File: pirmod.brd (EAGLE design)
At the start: 100 x 80 mm, 12 parts, among them IC1 TLC555CD, K1 22V, K2 LSP10, K3 LSP10

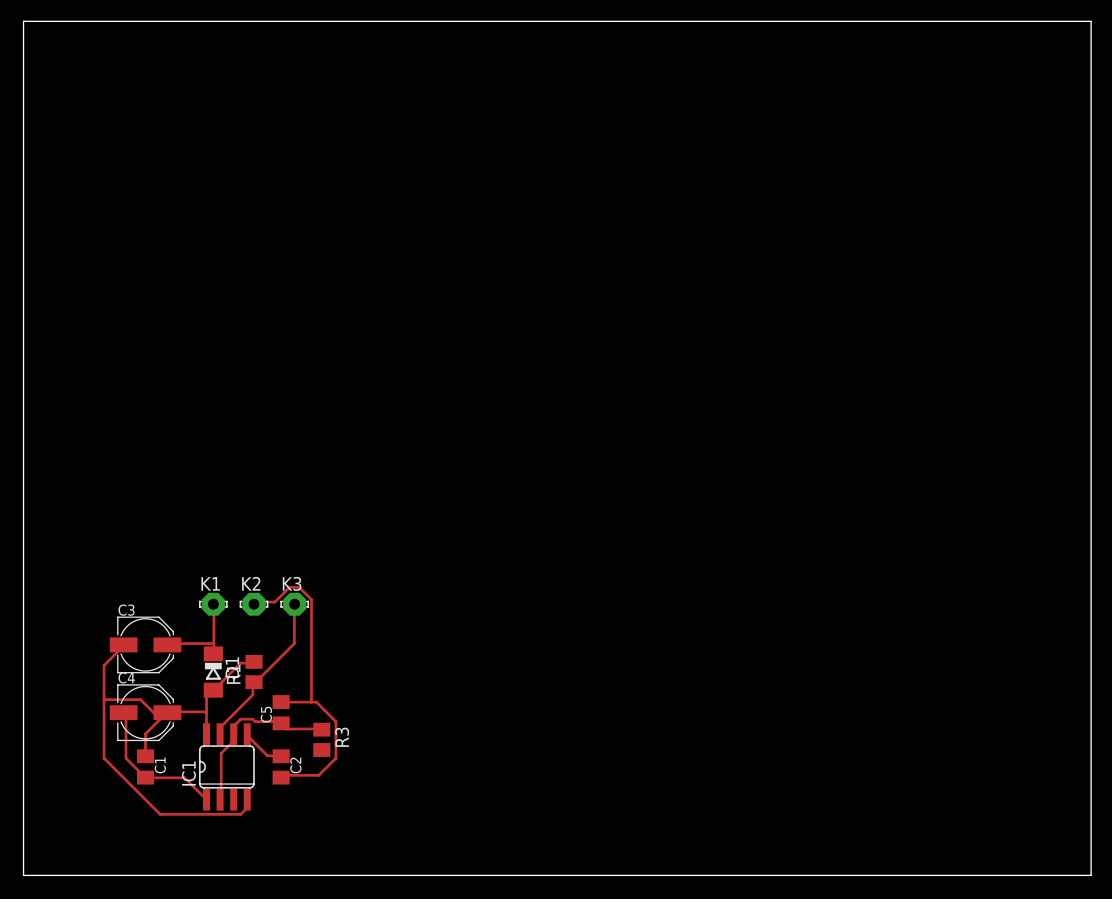
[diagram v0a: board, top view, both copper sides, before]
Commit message: Endstufe entfernt
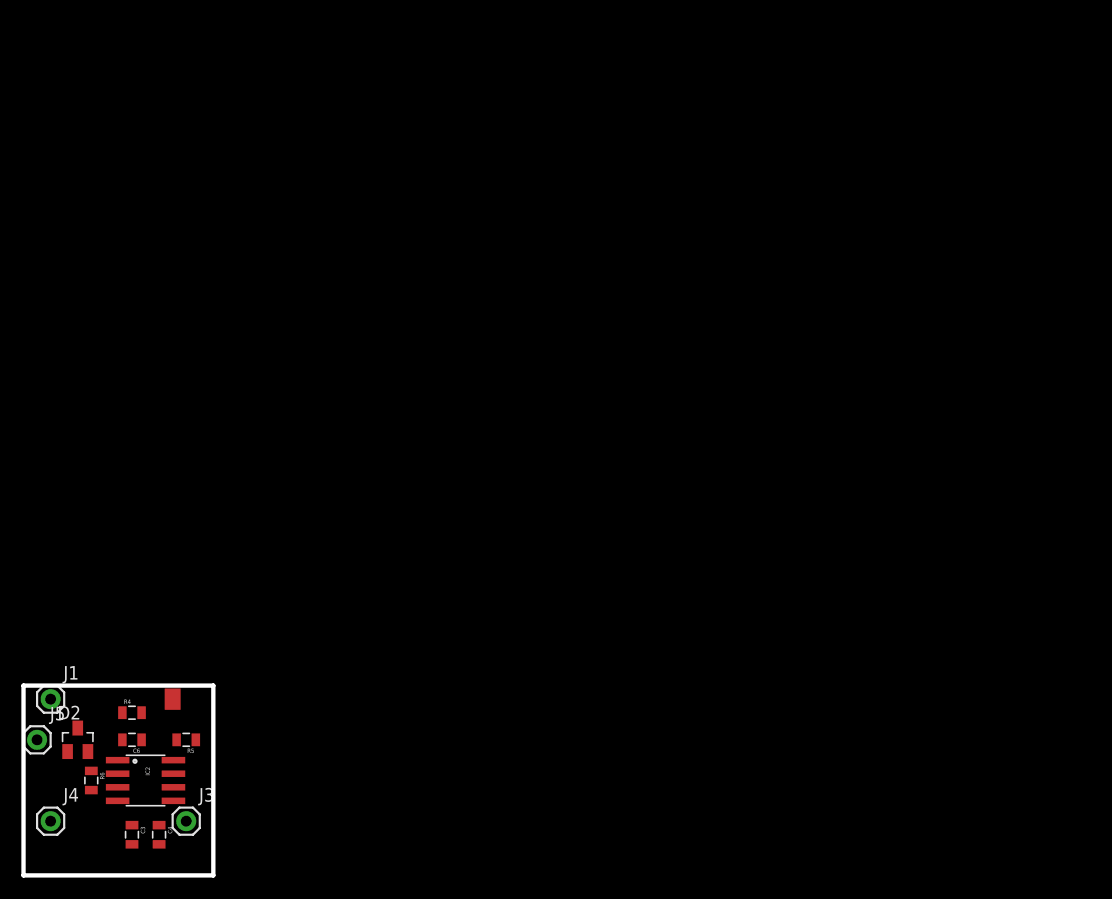
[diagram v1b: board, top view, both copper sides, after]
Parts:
- removed C1, C2, C5: 100n, rcl:C0805K
- removed D1: 12V/400mW, mahiso:SOD80C
- removed IC1: TLC555CD, mahiso:SO08
- removed K1: 22V, solpad:LSP10
- removed K2, K3: LSP10, solpad:LSP10
- removed R1: 4.7k, rcl:M0805
- removed R3: 68k, rcl:M0805
- added C6: 100n, SparkFun-Capacitors:0805
- added D2: BCX84-C12, diode:SOT23
- added IC2: TLC555, SparkFun-AnalogIC:SO08
- added J1: 22V, SparkFun-Connectors:1X01
- added J2: GND, SparkFun-Connectors:PAD-1.5X4.5
- added J3: TACT, SparkFun-Connectors:1X01
- added J4: OUT-PIR, SparkFun-Connectors:1X01
- added J5: OUT, SparkFun-Connectors:1X01
- added R4: 2,2k, SparkFun-Passives:0805
- added R5: 4,7k, SparkFun-Passives:0805
- added R6: 27k, SparkFun-Passives:0805
- C3, C4: value 10Âµ/35V -> 100n; device rcl:PANASONIC_C -> SparkFun-Capacitors:0805
- moved C3 17.8 mm to (10.2, 3.81), turned to 270 degrees
- moved C4 11.5 mm to (12.7, 3.81), turned to 270 degrees
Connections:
- removed net N$2: C2.1, IC1.5
- removed net N$6: IC1.3, R3.2
- removed net TAKT: IC1.7, K3.MP, R1.1
- removed net V+: C1.1, C3.-, C4.+, D1.A, IC1.4, IC1.8, R1.2
- removed net V+22V: C3.+, D1.C, K1.MP
- new net 12V: C6.1, D2.3, IC2.4, IC2.8, R4.2, R5.2
- new net N$3: C3.1, IC2.2, IC2.6, R6.1
- new net N$5: J1.1, R4.1
- new net N$7: C4.1, IC2.5
- new net N$8: IC2.3, R6.2
- new net N$9: IC2.7, J3.1, R5.1
- net GND: now also C3.2, C4.2, C6.2, D2.1, IC2.1, J2.P$1; no longer C1.2, C2.2, C4.-, C5.2, IC1.1, K2.MP
- net N$1: now also J4.1, J5.1; no longer C5.1, IC1.2, IC1.6, R3.1
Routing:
- net V+: track 53.0 -> 0.00 mm
- net GND: track 44.9 -> 0.00 mm
- net N$1: track 16.5 -> 0.00 mm
- net TAKT: track 15.2 -> 0.00 mm
- net V+22V: track 9.17 -> 0.00 mm
- net N$2: track 4.08 -> 0.00 mm
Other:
- board size 100 x 80 mm -> 17.8 x 17.8 mm

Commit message: Erstes Routing.
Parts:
- moved J1 0.51 mm to (2.54, 16.0)
- moved J2 0.25 mm to (14.0, 16.3)
- moved J5 0.25 mm to (1.52, 12.7)
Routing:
- net 12V: track 0.00 -> 24.4 mm
- net N$3: track 0.00 -> 13.2 mm
- net N$9: track 0.00 -> 12.0 mm
- net GND: track 0.00 -> 9.92 mm, vias 0 -> 4
- net N$1: track 0.00 -> 8.04 mm
- net N$5: track 0.00 -> 7.04 mm
- net N$7: track 0.00 -> 2.87 mm
- net N$8: track 0.00 -> 2.58 mm
- added copper zone on layer 16, net GND

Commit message: V1
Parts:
- D2: device diode:SOT23 -> SparkFun-DiscreteSemi:SOT23-3
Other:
- board text added: "mahiso.de PIRmod V1"
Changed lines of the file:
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@@
 <wire x1="17.78" y1="17.78" x2="17.78" y2="0" width="0.4064" layer="20"/>
 <wire x1="17.78" y1="0" x2="0" y2="0" width="0.4064" layer="20"/>
+<text x="1.016" y="0.762" size="0.6096" layer="25" font="vector">mahiso.de PIRmod V1</text>
 </plain>
 <attributes>
@@
 </autorouter>
 <elements>
-<element name="C3" library="SparkFun-Capacitors" package="0805" value="100n" x="10.16" y="3.81" rot="R270"/>
-<element name="C4" library="SparkFun-Capacitors" package="0805" value="100n" x="12.7" y="3.81" rot="R270"/>
-<element name="C6" library="SparkFun-Capacitors" package="0805" value="100n" x="10.16" y="12.7" rot="R180"/>
-<element name="D2" library="diode" package="SOT23" value="BCX84-C12" x="5.08" y="12.7"/>
+<element name="C3" library="SparkFun-Capacitors" package="0805" value="100n" x="10.16" y="3.81" smashed="yes" rot="R270">
+<attribute name="NAME" x="8.6995" y="4.318" size="0.4064" layer="25" rot="R270"/>
+<attribute name="VALUE" x="8.763" y="4.826" size="0.4064" layer="27" rot="R270"/>
+</element>
+<element name="C4" library="SparkFun-Capacitors" package="0805" value="100n" x="12.7" y="3.81" smashed="yes" rot="R270">
+<attribute name="NAME" x="11.2395" y="4.318" size="0.4064" layer="25" rot="R270"/>
+<attribute name="VALUE" x="11.303" y="4.826" size="0.4064" layer="27" rot="R270"/>
+</element>
+<element name="C6" library="SparkFun-Capacitors" package="0805" value="100n" x="10.16" y="12.7" smashed="yes" rot="R180">
+<attribute name="NAME" x="8.382" y="12.8905" size="0.4064" layer="25" rot="R180"/>
+<attribute name="VALUE" x="11.176" y="14.097" size="0.4064" layer="27" rot="R180"/>
+</element>
+<element name="D2" library="SparkFun-DiscreteSemi" package="SOT23-3" value="BCX84-C12" x="5.08" y="12.7"/>
 <element name="IC2" library="SparkFun-AnalogIC" package="SO08" value="TLC555" x="11.43" y="8.89" rot="R270"/>
-<element name="J1" library="SparkFun-Connectors" package="1X01" value="22V" x="2.54" y="16.002"/>
+<element name="J1" library="SparkFun-Connectors" package="1X01" value="22V" x="2.54" y="16.002" smashed="yes">
+<attribute name="NAME" x="2.9718" y="14.0208" size="0.6096" layer="25"/>
+<attribute name="VALUE" x="1.27" y="12.827" size="0.6096" layer="27"/>
+</element>
 <element name="J2" library="SparkFun-Connectors" package="PAD-1.5X4.5" value="GND" x="13.97" y="16.256"/>
-<element name="J3" library="SparkFun-Connectors" package="1X01" value="TACT" x="15.24" y="5.08"/>
-<element name="J4" library="SparkFun-Connectors" package="1X01" value="OUT-PIR" x="2.54" y="5.08"/>
-<element name="J5" library="SparkFun-Connectors" package="1X01" value="OUT" x="1.524" y="12.7"/>
+<element name="J3" library="SparkFun-Connectors" package="1X01" value="TACT" x="15.24" y="5.08" smashed="yes">
+<attribute name="NAME" x="14.9098" y="2.8448" size="0.6096" layer="25"/>
+<attribute name="VALUE" x="13.97" y="1.905" size="0.6096" layer="27"/>
+</element>
+<element name="J4" library="SparkFun-Connectors" package="1X01" value="OUT-PIR" x="2.54" y="5.08" smashed="yes">
+<attribute name="NAME" x="2.2098" y="2.8448" size="0.6096" layer="25"/>
+<attribute name="VALUE" x="1.27" y="1.905" size="0.6096" layer="27"/>
+</element>
+<element name="J5" library="SparkFun-Connectors" package="1X01" value="OUT" x="1.524" y="12.7" smashed="yes">
+<attribute name="NAME" x="1.7018" y="10.4648" size="0.6096" layer="25"/>
+<attribute name="VALUE" x="0.254" y="9.525" size="0.6096" layer="27"/>
+</element>
 <element name="R4" library="SparkFun-Passives" package="0805" value="2,2k" x="10.16" y="15.24"/>
-<element name="R5" library="SparkFun-Passives" package="0805" value="4,7k" x="15.24" y="12.7" rot="R180"/>
-<element name="R6" library="SparkFun-Passives" package="0805" value="27k" x="6.35" y="8.89" rot="R270"/>
+<element name="R5" library="SparkFun-Passives" package="0805" value="4,7k" x="15.24" y="12.7" smashed="yes" rot="R180">
+<attribute name="NAME" x="15.494" y="14.1605" size="0.4064" layer="25" rot="R180"/>
+<attribute name="VALUE" x="16.256" y="14.097" size="0.4064" layer="27" rot="R180"/>
+</element>
+<element name="R6" library="SparkFun-Passives" package="0805" value="27k" x="6.35" y="8.89" smashed="yes" rot="R270">
+<attribute name="NAME" x="4.6355" y="9.144" size="0.4064" layer="25" rot="R270"/>
+<attribute name="VALUE" x="4.953" y="9.906" size="0.4064" layer="27" rot="R270"/>
+</element>
 </elements>
 <signals>
@@
 <wire x1="4.1148" y1="10.9728" x2="4.1148" y2="11.5824" width="0.1524" layer="1"/>
 <wire x1="3.556" y1="10.414" x2="4.1148" y2="10.9728" width="0.1524" layer="1"/>
-<wire x1="4.1148" y1="11.5824" x2="4.13" y2="11.6" width="0.1524" layer="1"/>
+<wire x1="4.1148" y1="11.5824" x2="4.13" y2="11.7" width="0.1524" layer="1"/>
 <wire x1="13.8684" y1="15.8496" x2="13.8684" y2="16.1544" width="0.1524" layer="1"/>
 <wire x1="13.2588" y1="15.24" x2="13.8684" y2="15.8496" width="0.1524" layer="1"/>
@@
 </signal>
 </signals>
+<errors>
+</errors>
 </board>
 </drawing>

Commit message: V1
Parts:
- moved J5 1.78 mm to (1.52, 10.9)
- moved J4 0.57 mm to (3.05, 4.83)
- moved J1 0.51 mm to (3.05, 16.0)
- moved J3 0.36 mm to (15.5, 4.83)
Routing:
- net N$1: track 8.04 -> 6.81 mm
- net GND: track 10.0 -> 8.81 mm
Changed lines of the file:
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@@
 <wire x1="17.78" y1="17.78" x2="17.78" y2="0" width="0.4064" layer="20"/>
 <wire x1="17.78" y1="0" x2="0" y2="0" width="0.4064" layer="20"/>
-<text x="1.016" y="0.762" size="0.6096" layer="25" font="vector">mahiso.de PIRmod V1</text>
+<text x="1.27" y="1.016" size="0.6096" layer="25" font="vector">mahiso.de PIRmod V1</text>
 </plain>
 <attributes>
@@
 <attribute name="VALUE" x="11.176" y="14.097" size="0.4064" layer="27" rot="R180"/>
 </element>
-<element name="D2" library="SparkFun-DiscreteSemi" package="SOT23-3" value="BCX84-C12" x="5.08" y="12.7"/>
+<element name="D2" library="SparkFun-DiscreteSemi" package="SOT23-3" value="BCX84-C12" x="5.08" y="12.7" smashed="yes">
+<attribute name="NAME" x="5.7785" y="14.224" size="0.4064" layer="25"/>
+<attribute name="VALUE" x="4.064" y="12.5095" size="0.4064" layer="27"/>
+</element>
 <element name="IC2" library="SparkFun-AnalogIC" package="SO08" value="TLC555" x="11.43" y="8.89" rot="R270"/>
-<element name="J1" library="SparkFun-Connectors" package="1X01" value="22V" x="2.54" y="16.002" smashed="yes">
-<attribute name="NAME" x="2.9718" y="14.0208" size="0.6096" layer="25"/>
-<attribute name="VALUE" x="1.27" y="12.827" size="0.6096" layer="27"/>
+<element name="J1" library="SparkFun-Connectors" package="1X01" value="22V" x="3.048" y="16.002" smashed="yes">
+<attribute name="NAME" x="2.2098" y="13.7668" size="0.6096" layer="25"/>
+<attribute name="VALUE" x="1.778" y="12.827" size="0.6096" layer="27"/>
 </element>
 <element name="J2" library="SparkFun-Connectors" package="PAD-1.5X4.5" value="GND" x="13.97" y="16.256"/>
-<element name="J3" library="SparkFun-Connectors" package="1X01" value="TACT" x="15.24" y="5.08" smashed="yes">
-<attribute name="NAME" x="14.9098" y="2.8448" size="0.6096" layer="25"/>
-<attribute name="VALUE" x="13.97" y="1.905" size="0.6096" layer="27"/>
-</element>
-<element name="J4" library="SparkFun-Connectors" package="1X01" value="OUT-PIR" x="2.54" y="5.08" smashed="yes">
-<attribute name="NAME" x="2.2098" y="2.8448" size="0.6096" layer="25"/>
-<attribute name="VALUE" x="1.27" y="1.905" size="0.6096" layer="27"/>
-</element>
-<element name="J5" library="SparkFun-Connectors" package="1X01" value="OUT" x="1.524" y="12.7" smashed="yes">
-<attribute name="NAME" x="1.7018" y="10.4648" size="0.6096" layer="25"/>
-<attribute name="VALUE" x="0.254" y="9.525" size="0.6096" layer="27"/>
+<element name="J3" library="SparkFun-Connectors" package="1X01" value="TACT" x="15.494" y="4.826" smashed="yes">
+<attribute name="NAME" x="15.1638" y="2.5908" size="0.6096" layer="25"/>
+<attribute name="VALUE" x="14.224" y="1.651" size="0.6096" layer="27"/>
+</element>
+<element name="J4" library="SparkFun-Connectors" package="1X01" value="OUT-PIR" x="3.048" y="4.826" smashed="yes">
+<attribute name="NAME" x="2.7178" y="2.5908" size="0.6096" layer="25"/>
+<attribute name="VALUE" x="1.778" y="1.651" size="0.6096" layer="27"/>
+</element>
+<element name="J5" library="SparkFun-Connectors" package="1X01" value="OUT" x="1.524" y="10.922" smashed="yes">
+<attribute name="NAME" x="1.7018" y="8.6868" size="0.6096" layer="25"/>
+<attribute name="VALUE" x="0.254" y="7.747" size="0.6096" layer="27"/>
 </element>
 <element name="R4" library="SparkFun-Passives" package="0805" value="2,2k" x="10.16" y="15.24"/>
@@
 <vertex x="17.78" y="0"/>
 </polygon>
-<via x="13.208" y="15.24" extent="1-16" drill="0.6" shape="square"/>
-<via x="10.414" y="10.922" extent="1-16" drill="0.6" shape="square"/>
-<via x="3.556" y="10.414" extent="1-16" drill="0.6" shape="square"/>
-<via x="9.144" y="2.794" extent="1-16" drill="0.6" shape="square"/>
+<via x="13.208" y="15.24" extent="1-16" drill="0.5"/>
+<via x="10.414" y="10.922" extent="1-16" drill="0.5"/>
+<via x="4.064" y="10.668" extent="1-16" drill="0.5"/>
 <wire x1="9.144" y1="11.1252" x2="9.144" y2="12.6492" width="0.1524" layer="1"/>
 <wire x1="8.8138" y1="10.795" x2="9.144" y2="11.1252" width="0.1524" layer="1"/>
 <wire x1="9.144" y1="12.6492" x2="9.26" y2="12.7" width="0.1524" layer="1"/>
-<wire x1="9.144" y1="2.8956" x2="10.0584" y2="2.8956" width="0.1524" layer="1"/>
 <wire x1="10.0584" y1="2.8956" x2="10.16" y2="2.91" width="0.1524" layer="1"/>
-<wire x1="9.144" y1="2.8956" x2="9.144" y2="2.794" width="0.1524" layer="1"/>
-<wire x1="10.2108" y1="2.8956" x2="12.6492" y2="2.8956" width="0.1524" layer="1"/>
 <wire x1="12.6492" y1="2.8956" x2="12.7" y2="2.91" width="0.1524" layer="1"/>
 <wire x1="10.2108" y1="2.8956" x2="10.16" y2="2.91" width="0.1524" layer="1"/>
 <wire x1="4.1148" y1="10.9728" x2="4.1148" y2="11.5824" width="0.1524" layer="1"/>
-<wire x1="3.556" y1="10.414" x2="4.1148" y2="10.9728" width="0.1524" layer="1"/>
+<wire x1="4.064" y1="10.668" x2="4.1148" y2="10.9728" width="0.1524" layer="1"/>
 <wire x1="4.1148" y1="11.5824" x2="4.13" y2="11.7" width="0.1524" layer="1"/>
 <wire x1="13.8684" y1="15.8496" x2="13.8684" y2="16.1544" width="0.1524" layer="1"/>
@@
 <wire x1="10.2108" y1="11.1252" x2="9.144" y2="11.1252" width="0.1524" layer="1"/>
 <wire x1="10.414" y1="10.922" x2="10.2108" y2="11.1252" width="0.1524" layer="1"/>
+<via x="11.43" y="3.048" extent="1-16" drill="0.5"/>
+<wire x1="11.43" y1="3.048" x2="10.2108" y2="3.048" width="0.1524" layer="1"/>
+<wire x1="10.2108" y1="3.048" x2="10.16" y2="2.91" width="0.1524" layer="1"/>
+<wire x1="12.6492" y1="3.048" x2="11.43" y2="3.048" width="0.1524" layer="1"/>
+<wire x1="12.6492" y1="3.048" x2="12.7" y2="2.91" width="0.1524" layer="1"/>
 </signal>
 <signal name="N$3">
@@
 <wire x1="14.1732" y1="9.6012" x2="14.0462" y2="9.525" width="0.1524" layer="1"/>
 <wire x1="15.9004" y1="5.334" x2="15.9004" y2="9.6012" width="0.1524" layer="1"/>
-<wire x1="15.24" y1="5.1816" x2="15.9004" y2="5.334" width="0.1524" layer="1"/>
 <wire x1="15.9004" y1="9.6012" x2="14.0462" y2="9.525" width="0.1524" layer="1"/>
-<wire x1="15.24" y1="5.1816" x2="15.24" y2="5.08" width="0.1524" layer="1"/>
+<wire x1="15.8496" y1="5.1816" x2="15.494" y2="4.826" width="0.1524" layer="1"/>
+<wire x1="15.8496" y1="5.334" x2="15.8496" y2="5.1816" width="0.1524" layer="1"/>
+<wire x1="15.8496" y1="5.334" x2="15.9004" y2="5.334" width="0.1524" layer="1"/>
 </signal>
 <signal name="12V">
@@
 <contactref element="J1" pad="1"/>
 <wire x1="3.3528" y1="15.24" x2="9.26" y2="15.24" width="0.1524" layer="1"/>
-<wire x1="2.5908" y1="16.002" x2="3.3528" y2="15.24" width="0.1524" layer="1"/>
-<wire x1="2.5908" y1="16.002" x2="2.54" y2="16.002" width="0.1524" layer="1"/>
+<wire x1="3.3528" y1="15.6972" x2="3.3528" y2="15.24" width="0.1524" layer="1"/>
+<wire x1="3.048" y1="16.002" x2="3.3528" y2="15.6972" width="0.1524" layer="1"/>
 </signal>
 <signal name="N$1">
 <contactref element="J4" pad="1"/>
 <contactref element="J5" pad="1"/>
-<wire x1="1.524" y1="6.096" x2="1.524" y2="12.7" width="0.1524" layer="1"/>
-<wire x1="2.54" y1="5.08" x2="1.524" y2="6.096" width="0.1524" layer="1"/>
+<wire x1="1.524" y1="6.096" x2="1.524" y2="10.922" width="0.1524" layer="1"/>
+<wire x1="3.048" y1="4.826" x2="1.524" y2="6.096" width="0.1524" layer="1"/>
 </signal>
 </signals>
